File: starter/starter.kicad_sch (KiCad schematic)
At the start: 31 parts, among them J1 Conn_01x04_MountingPin, J2 Conn_01x02, Q1 Q_NMOS_GDS, U1 MCP1416, U2 LM1117DT-ADJ, U3 TLC555xD

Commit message: Add start pcb
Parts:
- added H1, H2, H3, H4: MountingHole, MountingHole:MountingHole_3.2mm_M3_Pad_Via, symbol Mechanical:MountingHole
- C1, C10, C2, C3, C4, C7: footprint (none) -> Capacitor_SMD:C_0805_2012Metric
- C11: footprint (none) -> Capacitor_Tantalum_SMD:CP_EIA-7343-31_Kemet-D
- C5, C6: footprint (none) -> Capacitor_THT:CP_Radial_D18.0mm_P7.50mm
- C8, C9: footprint (none) -> Capacitor_THT:CP_Radial_D10.0mm_P5.00mm
- D1, D2, D5: footprint (none) -> Diode_SMD:D_MiniMELF
- D3: footprint (none) -> Diode_SMD:D_SMC
- D4, Q1: footprint (none) -> Package_TO_SOT_SMD:TO-263-2
- J1: footprint (none) -> Connector_JST:JST_PH_S4B-PH-SM4-TB_1x04-1MP_P2.00mm_Horizontal
- J2: footprint (none) -> Connector_JST:JST_NV_B02P-NV_1x02_P5.00mm_Vertical
- R1, R2, R3, R5, R7, R8: footprint (none) -> Resistor_SMD:R_0805_2012Metric
- R4, R6: footprint (none) -> Resistor_SMD:R_2512_6332Metric
- RV1: footprint (none) -> Potentiometer_SMD:Potentiometer_Bourns_3214W_Vertical
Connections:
- net VCC is gone; now on net +12V: J1.2 (Pin_2)

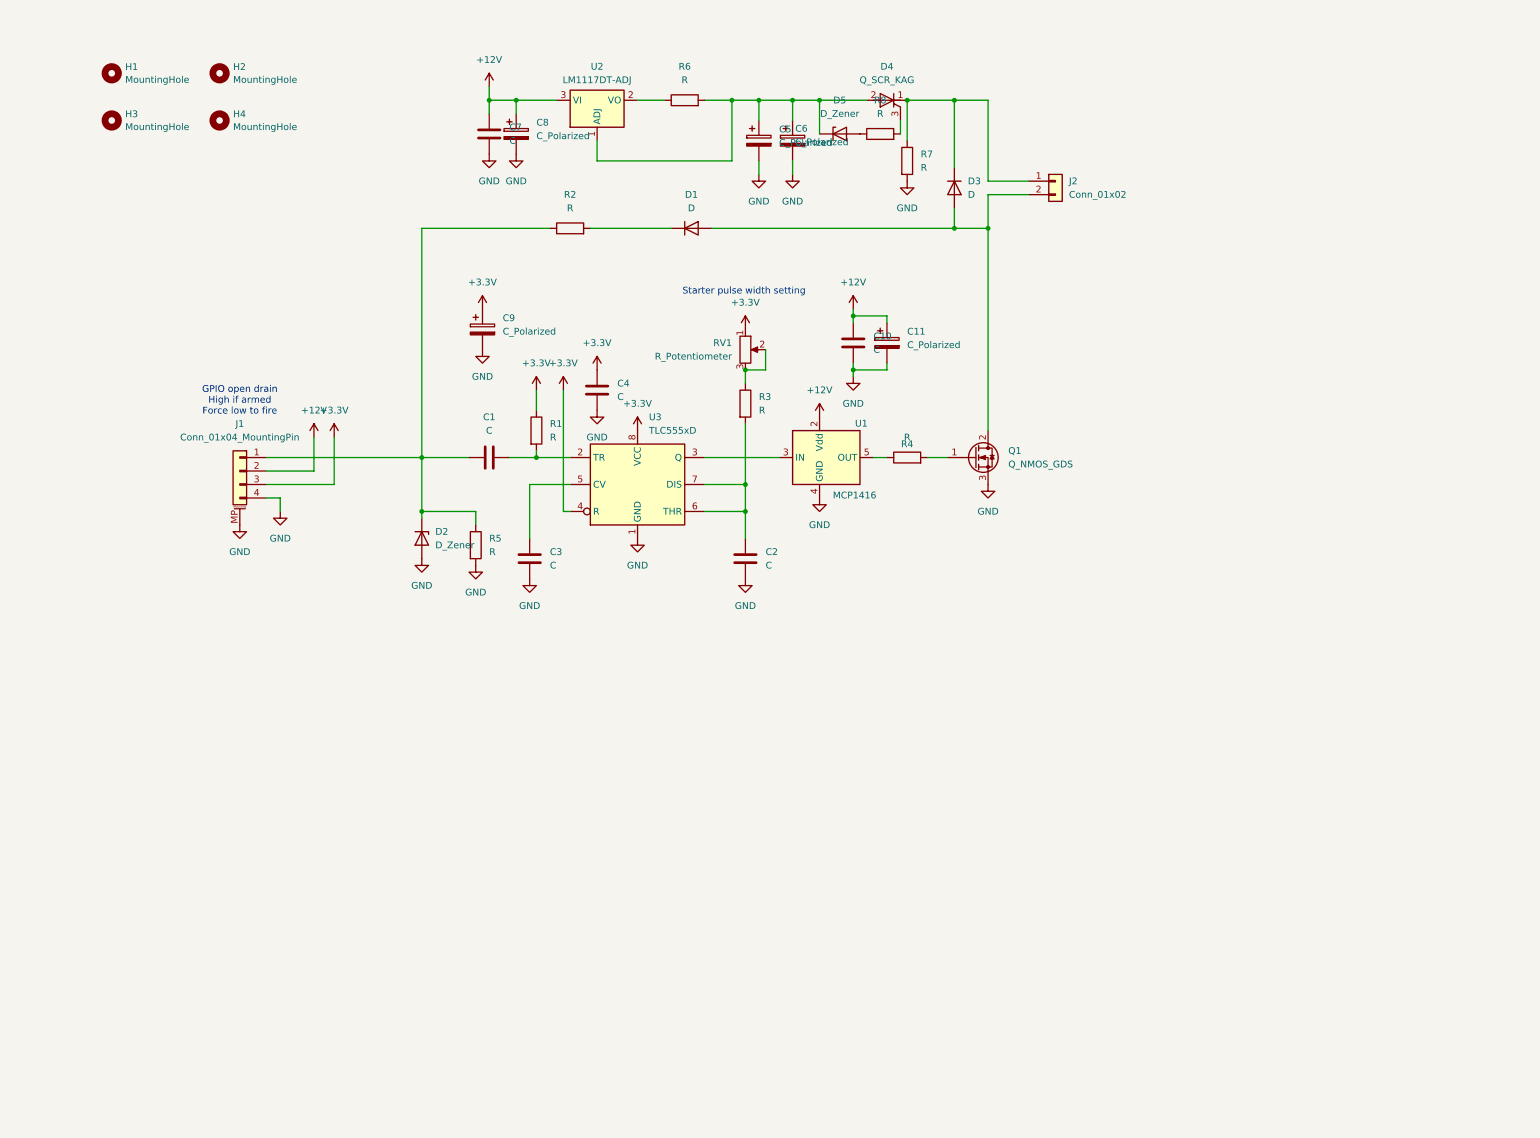
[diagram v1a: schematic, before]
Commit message: Update starter to rev 2 with I2C IO expander
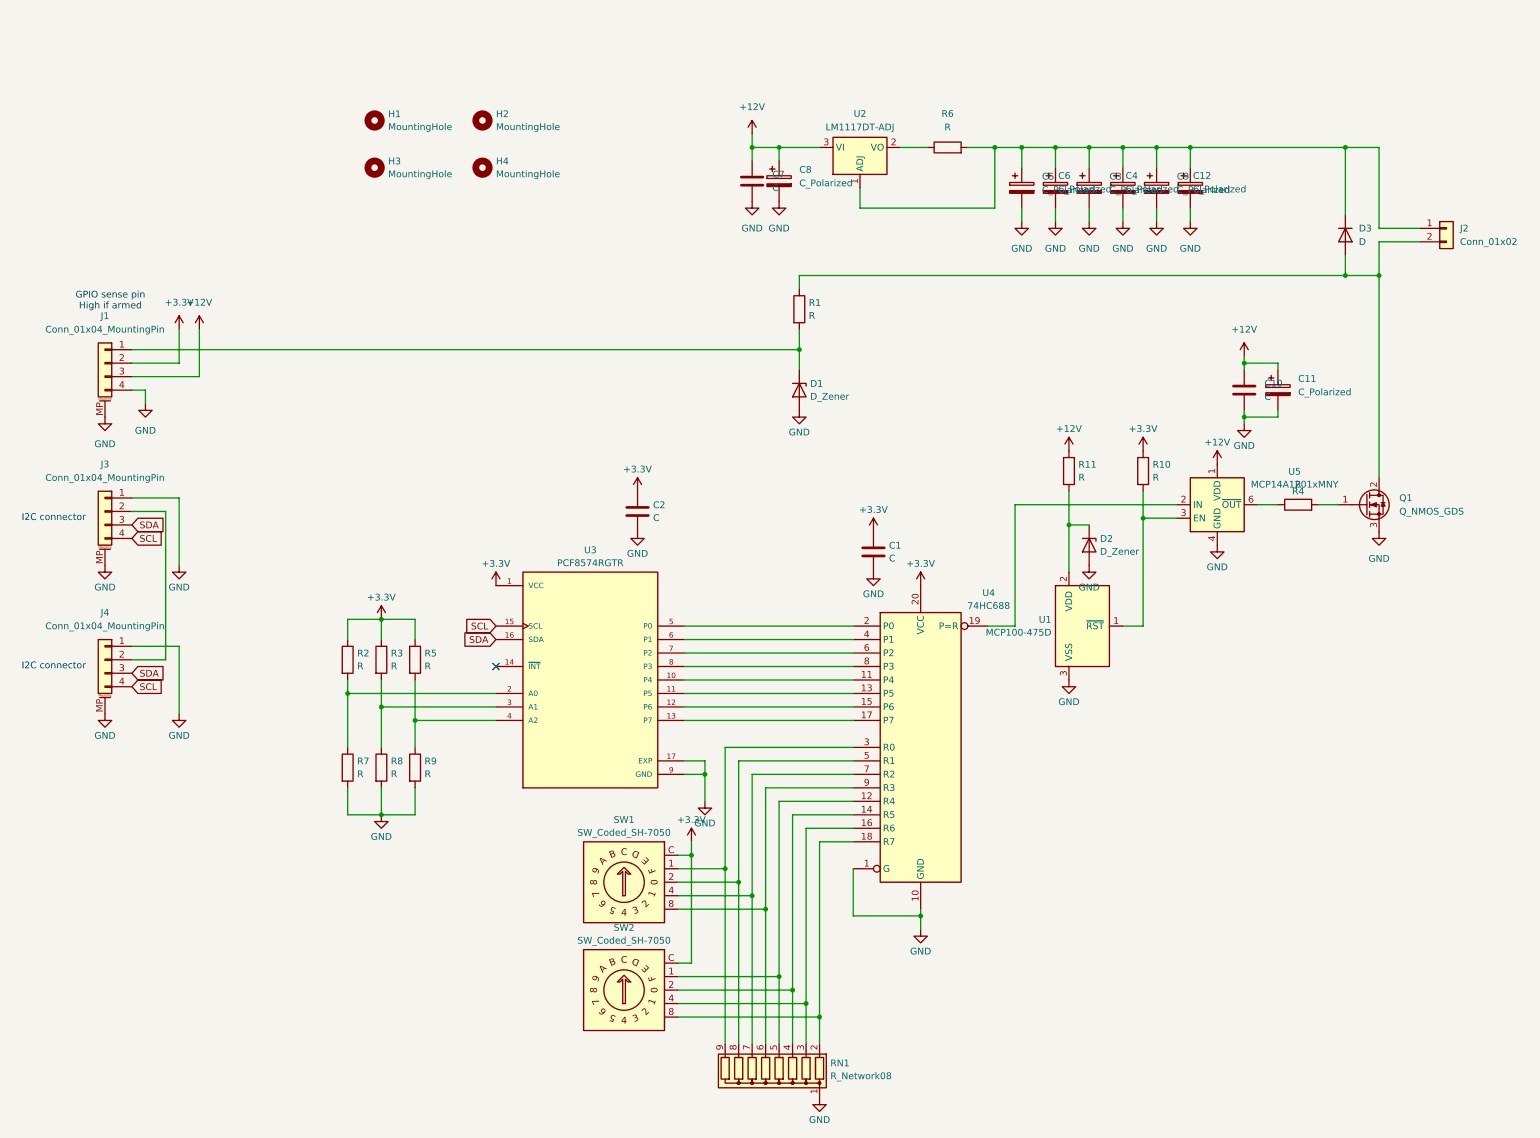
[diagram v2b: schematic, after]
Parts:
- removed C3, C4: C, Capacitor_SMD:C_0805_2012Metric, symbol Device:C
- removed D1: D, Diode_SMD:D_MiniMELF, symbol Device:D
- removed D4: Q_SCR_KAG, Package_TO_SOT_SMD:TO-263-2, symbol Device:Q_SCR_KAG
- removed D5: D_Zener, Diode_SMD:D_MiniMELF, symbol Device:D_Zener
- removed RV1: R_Potentiometer, Potentiometer_SMD:Potentiometer_Bourns_3214W_Vertical, symbol Device:R_Potentiometer
- removed U1: MCP1416, Package_TO_SOT_SMD:SOT-23-5, symbol Driver_FET:MCP1416
- removed U3: TLC555xD, Package_SO:SOIC-8_3.9x4.9mm_P1.27mm, symbol Timer:TLC555xD
- added C12, C3, C4: C_Polarized, Capacitor_THT:CP_Radial_D18.0mm_P7.50mm, symbol Device:C_Polarized
- added D1: D_Zener, Diode_SMD:D_MiniMELF, symbol Device:D_Zener
- added J3, J4: Conn_01x04_MountingPin, Connector_JST:JST_PH_S4B-PH-SM4-TB_1x04-1MP_P2.00mm_Horizontal, symbol Connector_Generic_MountingPin:Conn_01x04_MountingPin
- added R10, R11, R9: R, Resistor_SMD:R_0805_2012Metric, symbol Device:R
- added RN1: R_Network08, Resistor_THT:R_Array_SIP9, symbol Device:R_Network08
- added SW1, SW2: SW_Coded_SH-7050, Button_Switch_SMD:Nidec_Copal_SH-7010A, symbol Switch:SW_Coded_SH-7050
- added U1: MCP100-475D, Package_TO_SOT_SMD:SOT-23, symbol Power_Supervisor:MCP100-475D
- added U3: PCF8574RGTR, th:QFN50P300X300X100-17N, symbol PCF8574RGTR:PCF8574RGTR
- added U4: 74HC688, Package_SO:SOIC-20W_7.5x12.8mm_P1.27mm, symbol 74xx:74HC688
- added U5: MCP14A1201xMNY, Package_DFN_QFN:TDFN-8-1EP_3x2mm_P0.5mm_EP1.3x1.4mm, symbol Driver_FET:MCP14A1201xMNY
- C9: footprint Capacitor_THT:CP_Radial_D10.0mm_P5.00mm -> Capacitor_THT:CP_Radial_D18.0mm_P7.50mm
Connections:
- net +12V: now also J1.3 (Pin_3), R11.1, U5.1 (VDD), U5.8 (VDD); no longer J1.2 (Pin_2)
- net +3.3V: now also C1.1, C2.1, J1.2 (Pin_2), R2.1, R3.1, R5.1, R10.1, SW1.C, SW2.C, U3.1 (VCC), U4.20 (VCC); no longer C9.1, J1.3 (Pin_3), R1.1
- net GND: now also C1.2, R8.2, C12.2, C3.2, C4.2, D1.2 (A), J3.1 (Pin_1), J3.MP (MountPin), J4.1 (Pin_1), J4.MP (MountPin), R9.2, RN1.1 (common), U1.3 (VSS), U3.17 (EXP), U3.9 (GND), U4.1 (G), U4.10 (GND), U5.4 (GND), U5.5 (GND), U5.9 (GND); no longer R5.2
- net at R2.2: now also R7.1, U3.2 (A0)
- net at R8.1: now also R3.2, U3.3 (A1)
- net at R1.2: now also J1.1 (Pin_1), D1.1 (K); no longer C1.2
- net at C5.1, C6.1, R6.2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: now also C9.1, D3.1 (K), J2.1 (Pin_1), C12.1, C3.1, C4.1
- net at R4.1: now also U5.6 (~{OUT}), U5.7 (~{OUT})
- net at D3.2 (A), J2.2 (Pin_2), Q1.2 (D): now also R1.1
- new net: RN1.2 (R1), SW2.8, U4.18 (R7)
- new net: RN1.3 (R2), SW2.4, U4.16 (R6)
- new net: RN1.4 (R3), SW2.2, U4.14 (R5)
- new net: RN1.5 (R4), SW2.1, U4.12 (R4)
- new net: RN1.6 (R5), SW1.8, U4.9 (R3)
- new net: RN1.7 (R6), SW1.4, U4.7 (R2)
- new net: RN1.8 (R7), SW1.2, U4.5 (R1)
- new net: RN1.9 (R8), SW1.1, U4.3 (R0)
- new net: R5.2, R9.1, U3.4 (A2)
- new net: R10.2, U1.1 (~{RST}), U5.3 (EN)
- new net: U3.10 (P4), U4.11 (P4)
- new net: U3.11 (P5), U4.13 (P5)
- new net: U3.12 (P6), U4.15 (P6)
- new net: U3.13 (P7), U4.17 (P7)
- new net: U4.19 (P=R), U5.2 (IN)
- new net: U3.5 (P0), U4.2 (P0)
- new net: U3.6 (P1), U4.4 (P1)
- new net: U3.7 (P2), U4.6 (P2)
- new net: U3.8 (P3), U4.8 (P3)
- new net: J3.2 (Pin_2), J4.2 (Pin_2)
- new net: D2.1 (K), R11.2, U1.2 (VDD)
- new net SCL: J3.4 (Pin_4), J4.4 (Pin_4), U3.15 (SCL)
- new net SDA: J3.3 (Pin_3), J4.3 (Pin_3), U3.16 (SDA)
- no-connect marks 0 -> 1
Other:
- note added: "GPIO sense pin High if armed"
- note added: "I2C connector"
- note removed: "GPIO open drain High if armed Force low to fire"
- note removed: "Starter pulse width setting"
- moved on the sheet: C10, C11, C5, C6, C7, C8, D3, H1, H2, H3, H4, J1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

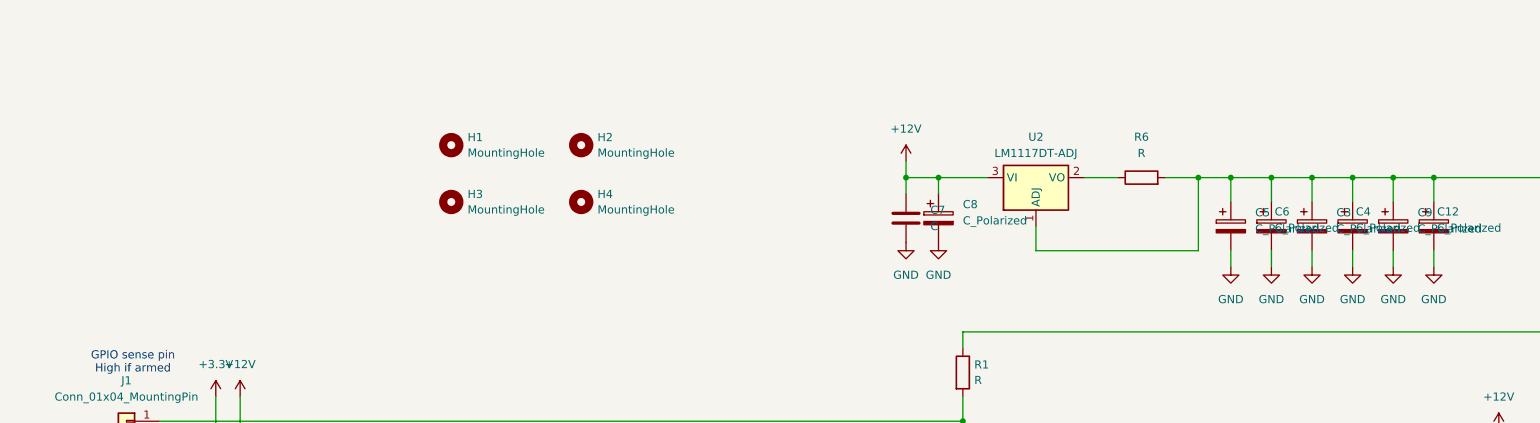
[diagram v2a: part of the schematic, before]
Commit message: Add high power connector
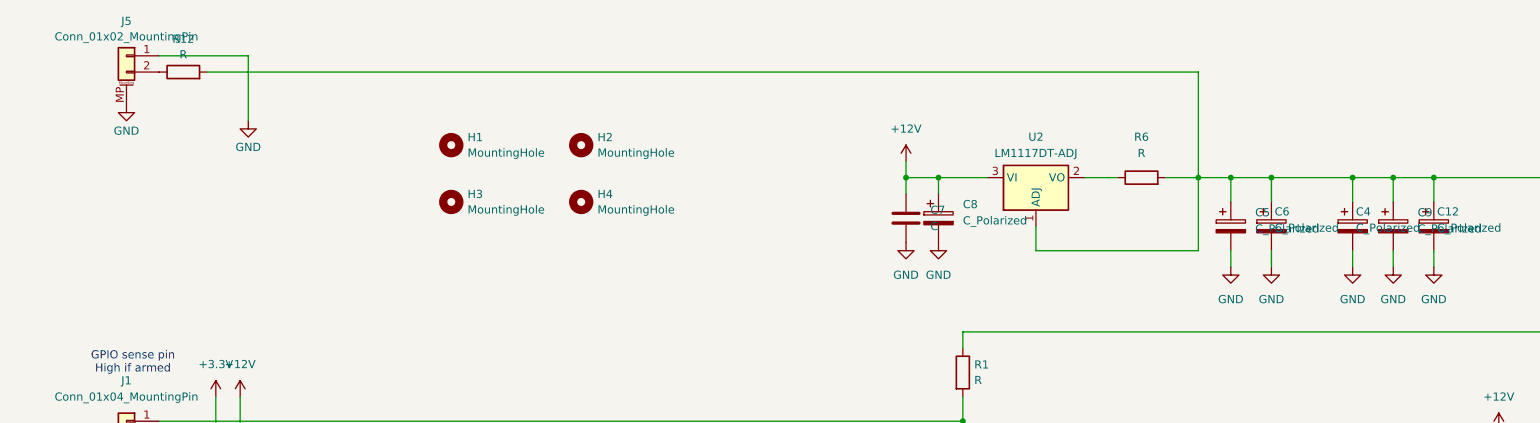
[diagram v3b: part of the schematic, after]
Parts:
- removed C3: C_Polarized, Capacitor_THT:CP_Radial_D18.0mm_P7.50mm, symbol Device:C_Polarized
- added J5: Conn_01x02_MountingPin, Connector_AMASS:AMASS_XT30PW-M_1x02_P2.50mm_Horizontal, symbol Connector_Generic_MountingPin:Conn_01x02_MountingPin
- added R12: R, Resistor_SMD:R_2512_6332Metric, symbol Device:R
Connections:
- net GND: now also J5.1 (Pin_1), J5.MP (MountPin)
- net at C12.1, C4.1, C5.1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: now also R12.2
- new net: J5.2 (Pin_2), R12.1

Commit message: Fix footprint for U1 in starter board
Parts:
- U1: footprint Package_TO_SOT_SMD:SOT-23 -> Package_TO_SOT_THT:TO-92L_Inline
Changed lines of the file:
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@@
 			)
 		)
-		(property "Footprint" "Package_TO_SOT_SMD:SOT-23"
+		(property "Footprint" "Package_TO_SOT_THT:TO-92L_Inline"
 			(at 208.28 129.54 0)
 			(effects

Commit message: Add value for some elements
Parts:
- C1, C10, C2, C7: value C -> 100nF
- C11: value C_Polarized -> 6.8uF
- D1: value D_Zener -> 3.3V zener
- D2: value D_Zener -> 5V zener
- R1, R10, R11: value R -> 10K
- R4: value R -> 2-10R
- RN1: value R_Network08 -> 10K
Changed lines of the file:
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@@
 			)
 		)
-		(property "Value" "R_Network08"
+		(property "Value" "10K"
 			(at 170.942 218.1281 0)
 			(effects
@@
 		(on_board yes)
 		(dnp no)
-		(fields_autoplaced yes)
 		(property "Reference" "C10"
-			(at 252.73 87.6299 0)
+			(at 242.57 84.836 0)
 			(effects
 				(font
@@
 			)
 		)
-		(property "Value" "C"
-			(at 252.73 90.1699 0)
+		(property "Value" "100nF"
+			(at 239.014 89.154 0)
 			(effects
 				(font
@@
 			)
 		)
-		(property "Value" "R"
+		(property "Value" "10K"
 			(at 166.878 74.8721 0)
 			(effects
@@
 			)
 		)
-		(property "Value" "C_Polarized"
+		(property "Value" "6.8uF"
 			(at 259.08 89.2809 0)
 			(effects
@@
 			)
 		)
-		(property "Value" "C"
+		(property "Value" "100nF"
 			(at 160.02 50.7999 0)
 			(effects
@@
 			)
 		)
-		(property "Value" "R"
-			(at 259.08 106.68 90)
+		(property "Value" "2-10R"
+			(at 259.334 113.538 90)
 			(effects
 				(font
@@
 			)
 		)
-		(property "Value" "R"
+		(property "Value" "10K"
 			(at 231.648 105.3521 0)
 			(effects
@@
 			)
 		)
-		(property "Value" "D_Zener"
+		(property "Value" "5V zener"
 			(at 221.742 119.3221 90)
 			(effects
@@
 			)
 		)
-		(property "Value" "R"
+		(property "Value" "10K"
 			(at 217.678 105.3521 0)
 			(effects
@@
 			)
 		)
-		(property "Value" "D_Zener"
+		(property "Value" "3.3V zener"
 			(at 167.132 90.1121 90)
 			(effects
@@
 		(on_board yes)
 		(dnp no)
-		(fields_autoplaced yes)
 		(property "Reference" "U5"
 			(at 258.411 104.2434 0)
@@
 		)
 		(property "Value" "MCP14A1201xMNY"
-			(at 258.411 106.6677 0)
+			(at 257.81 100.838 0)
 			(effects
 				(font
@@
 			)
 		)
-		(property "Value" "C"
+		(property "Value" "100nF"
 			(at 181.991 120.5921 0)
 			(effects
@@
 			)
 		)
-		(property "Value" "C"
+		(property "Value" "100nF"
 			(at 137.541 112.9721 0)
 			(effects

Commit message: updates
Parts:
- R2, R3, R5, R7, R8, R9: value R -> 0
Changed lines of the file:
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@@
 		(fields_autoplaced yes)
 		(property "Reference" "R5"
-			(at 94.488 138.4878 0)
+			(at 95.25 138.4299 0)
 			(effects
 				(font
@@
 			)
 		)
-		(property "Value" "R"
-			(at 94.488 140.9121 0)
+		(property "Value" "0"
+			(at 95.25 140.9699 0)
 			(effects
 				(font
@@
 		(fields_autoplaced yes)
 		(property "Reference" "R3"
-			(at 88.138 138.4878 0)
+			(at 88.9 138.4299 0)
 			(effects
 				(font
@@
 			)
 		)
-		(property "Value" "R"
-			(at 88.138 140.9121 0)
+		(property "Value" "0"
+			(at 88.9 140.9699 0)
 			(effects
 				(font
@@
 		(fields_autoplaced yes)
 		(property "Reference" "R9"
-			(at 94.488 158.8078 0)
+			(at 95.25 158.7499 0)
 			(effects
 				(font
@@
 			)
 		)
-		(property "Value" "R"
-			(at 94.488 161.2321 0)
+		(property "Value" "0"
+			(at 95.25 161.2899 0)
 			(effects
 				(font
@@
 		(fields_autoplaced yes)
 		(property "Reference" "R8"
-			(at 88.138 158.8078 0)
+			(at 88.9 158.7499 0)
 			(effects
 				(font
@@
 			)
 		)
-		(property "Value" "R"
-			(at 88.138 161.2321 0)
+		(property "Value" "0"
+			(at 88.9 161.2899 0)
 			(effects
 				(font
@@
 		(fields_autoplaced yes)
 		(property "Reference" "R2"
-			(at 81.788 138.4878 0)
+			(at 82.55 138.4299 0)
 			(effects
 				(font
@@
 			)
 		)
-		(property "Value" "R"
-			(at 81.788 140.9121 0)
+		(property "Value" "0"
+			(at 82.55 140.9699 0)
 			(effects
 				(font
@@
 		(fields_autoplaced yes)
 		(property "Reference" "R7"
-			(at 81.788 158.8078 0)
+			(at 82.55 158.7499 0)
 			(effects
 				(font
@@
 			)
 		)
-		(property "Value" "R"
-			(at 81.788 161.2321 0)
+		(property "Value" "0"
+			(at 82.55 161.2899 0)
 			(effects
 				(font
